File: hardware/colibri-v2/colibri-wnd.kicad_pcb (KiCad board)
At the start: 6 copper layers, 120 x 110 mm, 528 parts, among them CN1 XT60-M, CN10 629_105_150_921, CN11 629_105_150_921, CN12 XT60-F, CN2 XT60-F, CN3 AS0B821-S78B-7H, CN4 HDMI_A, CN5 692_121_030_100, CN6 Wurth-68715014522-LCD, CN7 MOLEX_73366_0061, CN8 629_105_150_921, CN9 Wurth-68711814522, CON1 PJ-102AH, P1 CONN_02X10, P10 CONN_01X08, P11 CONN_01X03, P12 CONN_01X03, P13 CONN_01X03, P14 CONN_01X03, P15 CONN_01X03, P16 CONN_01X03, P17 CONN_01X03, P18 CONN_01X03, P19 CONN_01X03, P20 CONN_01X03, P21 CONN_01X03, P22 CONN_01X03, P23 CONN_01X03, P24 CONN_01X03, P25 CONN_01X03, P26 CONN_01X03, P27 CONN_01X03, P28 CONN_01X03, P29 CONN_01X03, P3 CONN_02X01, P30 CONN_01X03, P31 CONN_01X03, P32 CONN_02X10, P33 ECM00870-L, P34 ECM00870-L, P35 STANDOFF, P36 STANDOFF, P37 STANDOFF, P38 STANDOFF, P39 STANDOFF, P4 ECM00870-L, P40 STANDOFF, P5 ECM00870-L, P6 CONN_01X08, P7 CONN_01X04, P8 CONN_01X04, P9 CONN_01X04, Q10 PDTC123JU, Q11 PDTA123JU, Q12 IRLML6402TRPBF, Q13 BSS138PW, Q14 PDTA123JU, Q15 BSS138PW, Q16 BSS138PW, Q17 IRLML6402TRPBF, Q3 BSS138PW, Q4 FDMA530PZ, Q5 BSS138PW, Q6 BSS138PW, Q7 BSS138PW, Q8 AP6681GMT-HF-3TR, Q9 FDMA530PZ, SW1 OMRON B3F-1070, SW10 OMRON B3F-1070, SW11 OMRON B3F-1070, SW2 OMRON B3F-1070, SW3 OMRON B3F-1070, SW4 OMRON B3F-1070, SW5 OMRON B3F-1070, SW6 OMRON B3F-1070, SW7 OMRON B3F-1070, SW8 OMRON B3F-1070, SW9 ALPS-SPPJ320600, U1 L3GD20HTR, U10 TPS2065CDBVT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

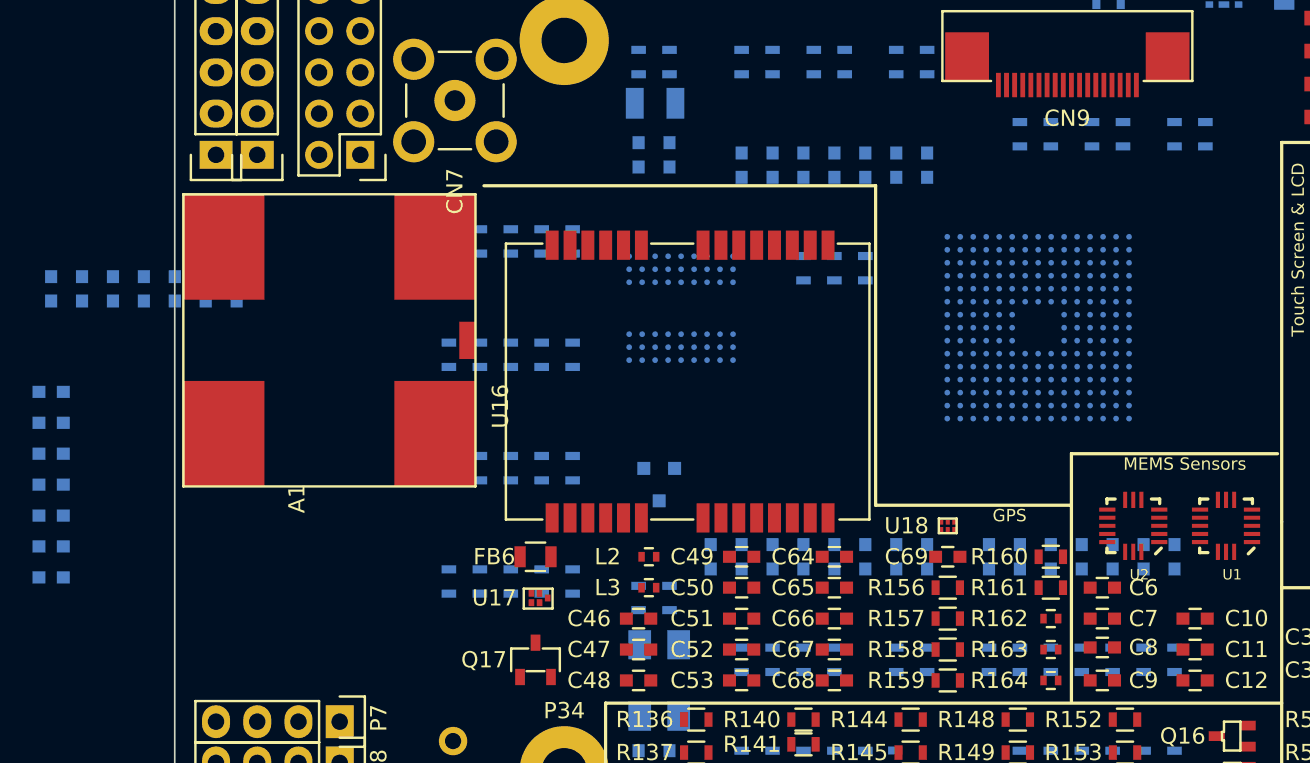
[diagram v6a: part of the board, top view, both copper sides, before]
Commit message: Fanned out all cortex pads
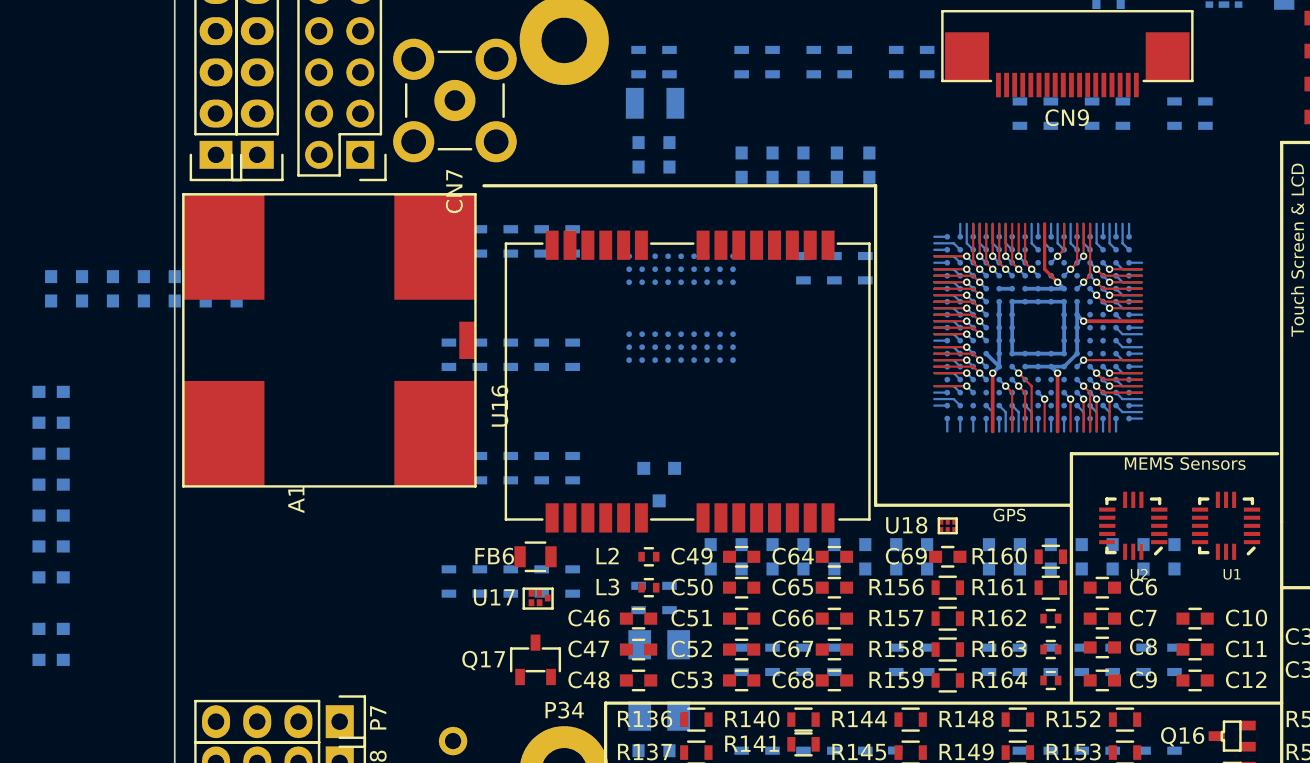
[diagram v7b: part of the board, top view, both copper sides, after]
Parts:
- moved C103 62.0 mm to (32.4, 113.7), turned to 180 degrees
- moved C100 59.4 mm to (32.4, 111.8), turned to 180 degrees
- moved C97 2.16 mm to (82.8, 83.2)
- moved C101 1.75 mm to (80.8, 83.2)
- moved R207 1.27 mm to (94.0, 80.0)
- moved R208 1.27 mm to (92.1, 80.0)
- moved R209 1.27 mm to (96.5, 80.0)
- moved R210 1.27 mm to (98.4, 80.0)
- moved R220 1.27 mm to (101.6, 80.0)
- moved R221 1.27 mm to (103.5, 80.0)
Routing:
- net +3V3: track 0.00 -> 32.9 mm, vias 0 -> 4
- net GND: track 0.00 -> 17.0 mm
- net /Leds/Buttons/BOOT0: track 0.00 -> 4.50 mm, vias 0 -> 1
- net /cortex/VCAP1: track 0.00 -> 4.33 mm, vias 0 -> 1
- net /cortex/VCAP2: track 0.00 -> 4.17 mm, vias 0 -> 1
- net /cortex/PI7: track 0.00 -> 3.53 mm, vias 0 -> 1
- net /STM32F4 SDRAM/FMC_SDNE0: track 0.00 -> 3.53 mm, vias 0 -> 1
- net /STM32F4 SDRAM/FMC_A11: track 0.00 -> 3.53 mm, vias 0 -> 1
- net /cortex/IN_PWM_03: track 0.00 -> 3.53 mm, vias 0 -> 1
- net /STM32F4 SDRAM/FMC_A9: track 0.00 -> 3.53 mm, vias 0 -> 1
- net /Power Control/BAT_MSRMNT: track 0.00 -> 3.53 mm, vias 0 -> 1
- net /Leds/Buttons/LED4: track 0.00 -> 3.53 mm, vias 0 -> 1
- net /External Sensors/C_I2C2_SCL: track 0.00 -> 3.53 mm, vias 0 -> 1
- net /cortex/PI9: track 0.00 -> 3.53 mm, vias 0 -> 1
- net /STM32F4 SDRAM/FMC_SDCKE0: track 0.00 -> 3.53 mm, vias 0 -> 1
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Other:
- net class Default: clearance 0.1016 -> 0.1; trace_width 0.127 -> 0.1397; via_dia 0.4826 -> 0.4572
- rule trace_clearance: 0.1016 -> 0.1
- rule trace_min: 0.1016 -> 0.0762

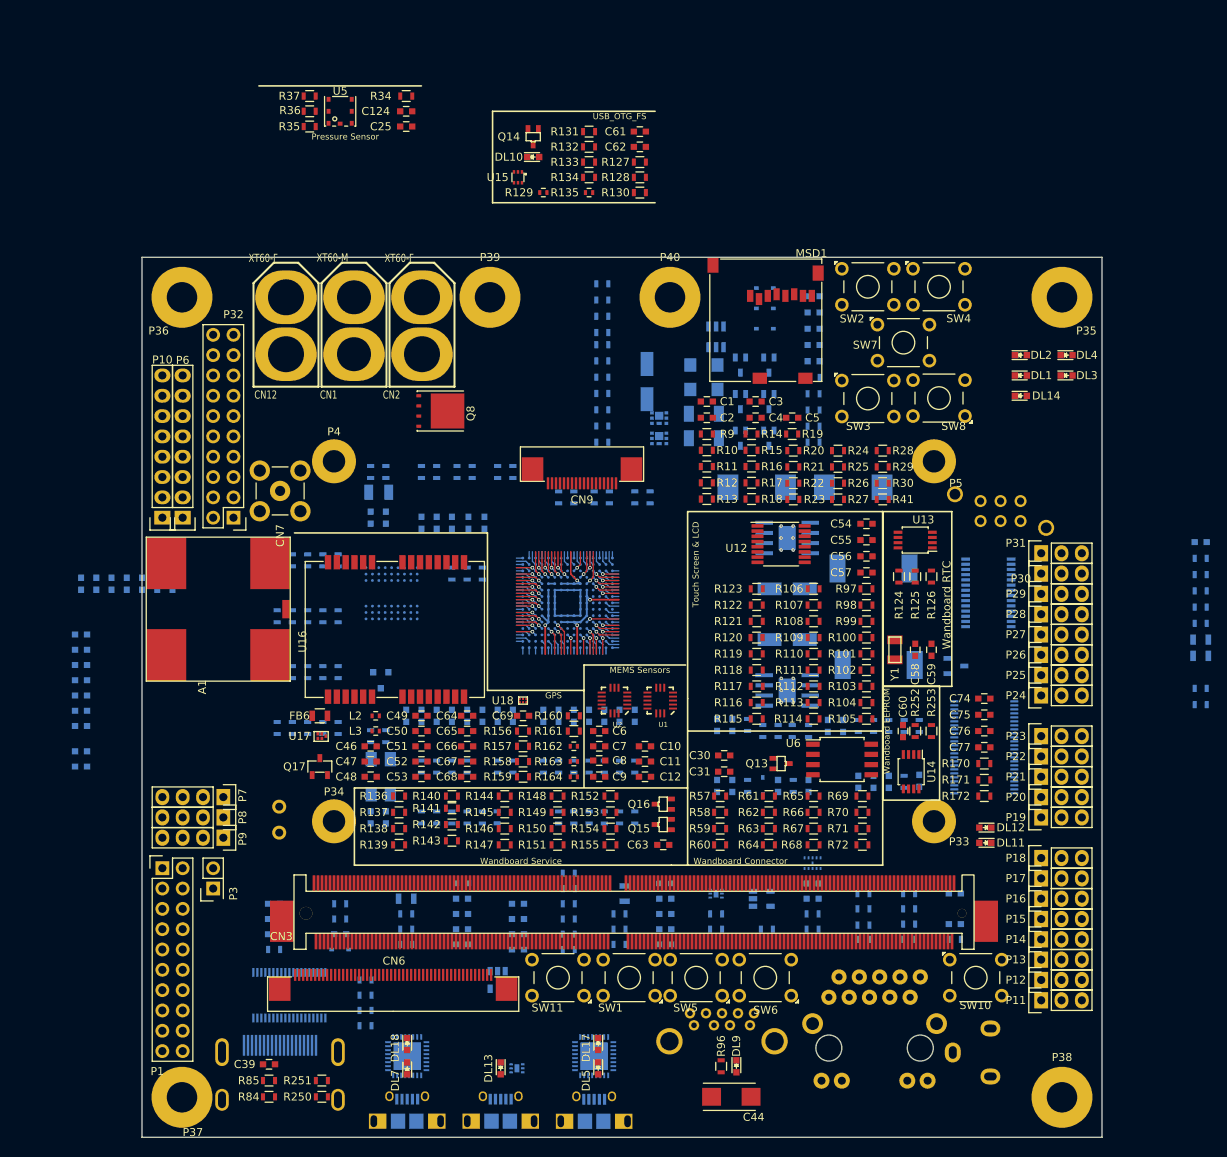
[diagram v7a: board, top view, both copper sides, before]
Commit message: Added power vias to cortex
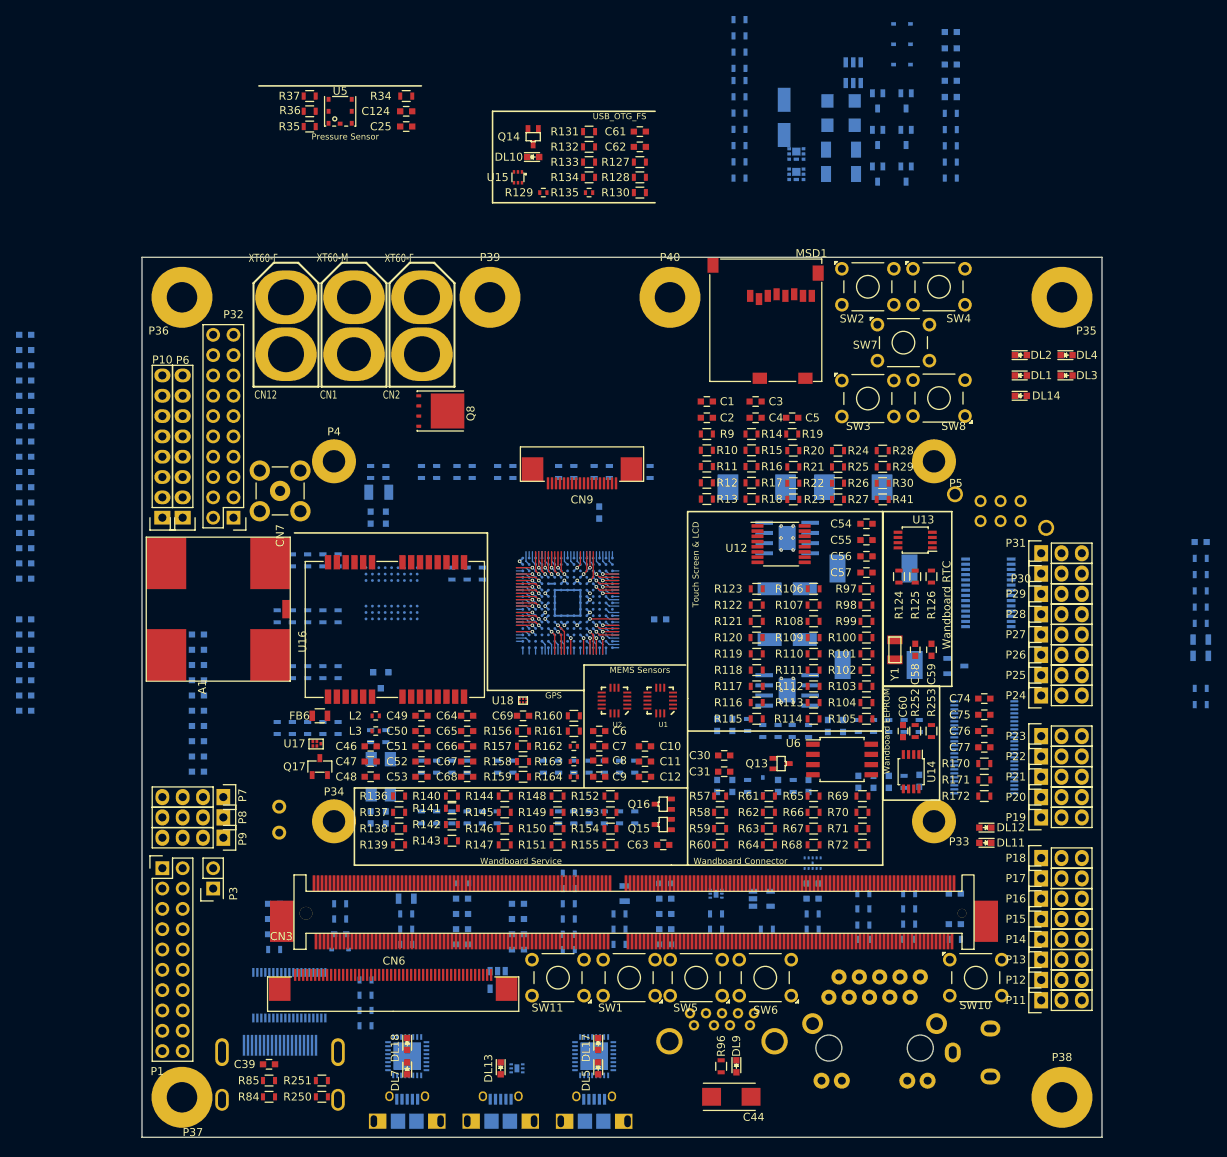
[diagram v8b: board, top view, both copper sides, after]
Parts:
- moved C115 83.5 mm to (25.4, 59.7), turned to 180 degrees
- moved C114 80.8 mm to (25.4, 61.6), turned to 180 degrees
- moved C113 78.2 mm to (25.4, 63.5), turned to 180 degrees
- moved C99 78.1 mm to (25.4, 90.2), turned to 0 degrees
- moved C102 77.7 mm to (25.4, 84.5), turned to 0 degrees
- moved C112 74.0 mm to (25.4, 65.4), turned to 180 degrees
- moved C111 68.2 mm to (25.4, 67.3), turned to 180 degrees
- moved C110 65.5 mm to (25.4, 69.2), turned to 180 degrees
- moved C109 62.9 mm to (25.4, 71.1), turned to 180 degrees
- moved C108 60.2 mm to (25.4, 73.0), turned to 180 degrees
- moved C107 57.6 mm to (25.4, 74.9), turned to 180 degrees
- moved C101 55.5 mm to (25.4, 86.4), turned to 180 degrees
- moved C104 53.4 mm to (25.4, 80.6), turned to 180 degrees
- moved C105 51.6 mm to (25.4, 78.7), turned to 180 degrees
- moved C96 51.1 mm to (47.0, 112.4), turned to 0 degrees
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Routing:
- net +3V3: track 32.9 -> 12.4 mm, vias 4 -> 12
- net /cortex/TIM1_CH3/FMC_D10: track 0.80 -> 0.00 mm
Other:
- net class Default: clearance 0.1 -> 0.09906; via_drill 0.254 -> 0.2286
- net class Power: via_dia 0.635 -> 0.762
- net class TFBGA added: clearance 0.09906, trace_width 0.1397, via_dia 0.4572, via_drill 0.2794
- rule trace_clearance: 0.1 -> 0.09906
